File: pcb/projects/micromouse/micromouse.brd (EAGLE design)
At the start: 80 x 100 mm, 45 parts, among them U1 DSPIC33FJ64MC804-H/PTTQFP44_1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, U2 UA78M33CKCS, U3 UA78M05CKCS

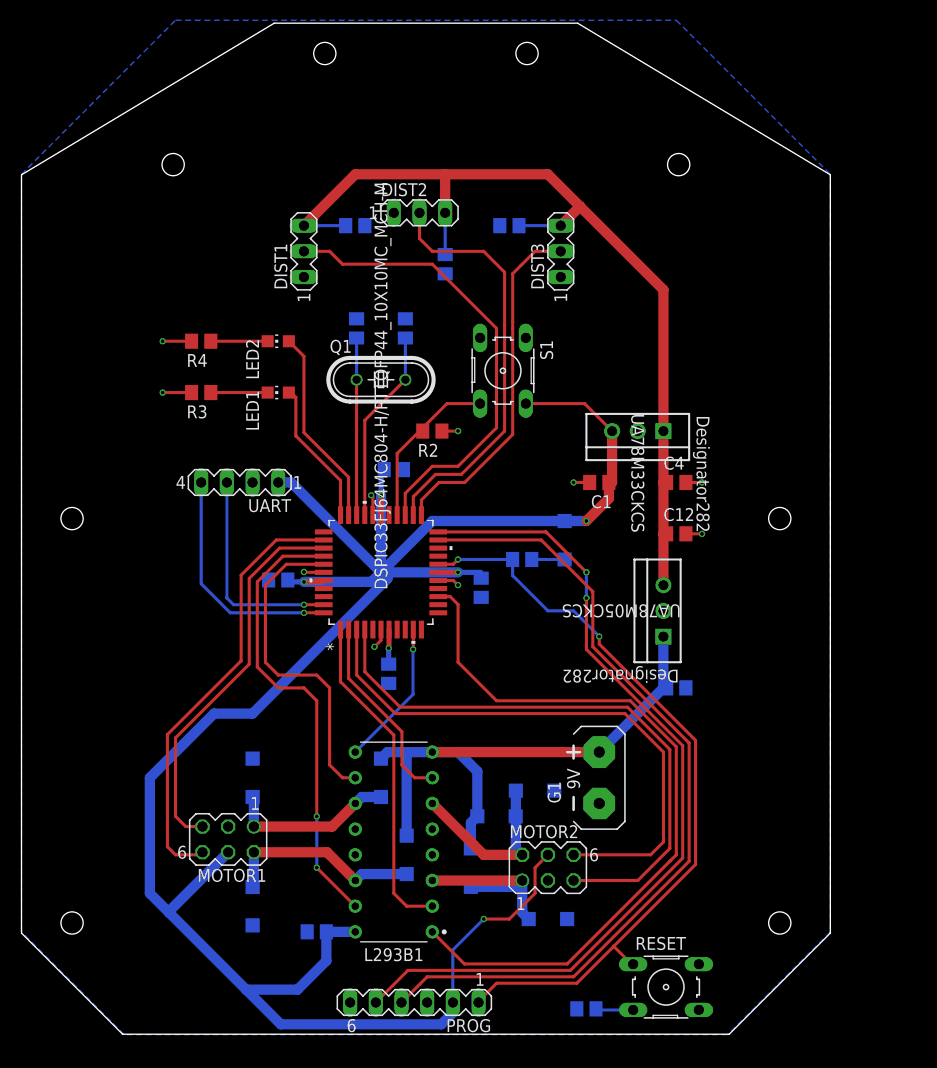
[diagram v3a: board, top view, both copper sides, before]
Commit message: Update reset button
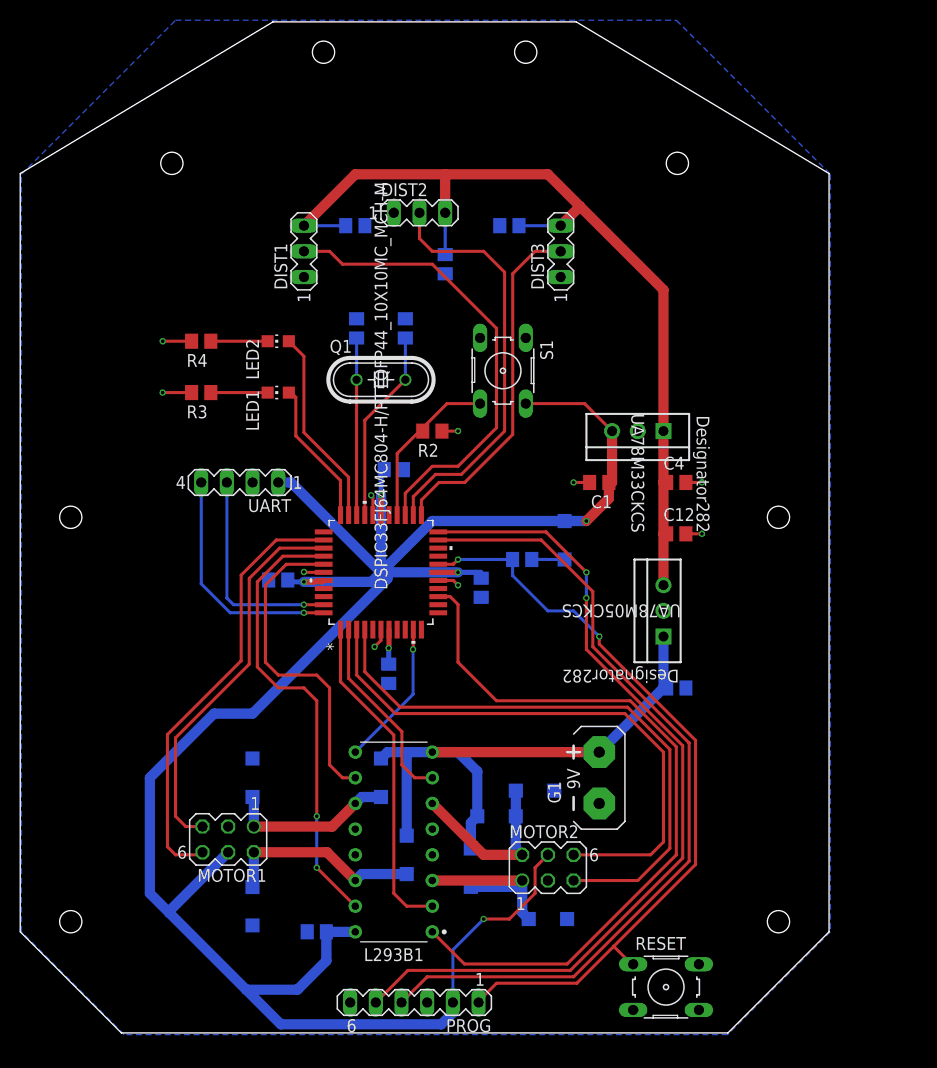
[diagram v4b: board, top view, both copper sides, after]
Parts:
- removed C8: 100nF, rcl:C0805
- R1: value 10k -> 47k
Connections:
- removed net N$3: C8.1, RESET.3
- net GND: now also RESET.3; no longer C8.2
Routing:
- net N$3: track 3.71 -> 0.00 mm
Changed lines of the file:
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@@
 <setting verticaltext="up"/>
 </settings>
-<grid distance="50" unitdist="mil" unit="mil" style="dots" multiple="1" display="yes" altdistance="5" altunitdist="mil" altunit="mil"/>
+<grid distance="50" unitdist="mil" unit="mm" style="dots" multiple="1" display="yes" altdistance="5" altunitdist="mil" altunit="mm"/>
 <layers>
 <layer number="1" name="Top" color="4" fill="1" visible="yes" active="yes"/>
@@
 </layers>
 <board>
-<fusionsync huburn="a.YnVzaW5lc3M6bXl0dW03NTE" projecturn="a.YnVzaW5lc3M6bXl0dW03NTEjMjAyMjAxMTg0ODY2MTA4MzE" f3durn="urn:adsk.wipprod:dm.lineage:keifWLGXSk6oYHrA5SEV4A" pcbguid="" lastpulledtime="2022-01-28T17:10:11Z" lastsyncedchangeguid="" latestrevisionid="4de54440-2fe9-4c7d-ae27-a806fae1d480" lastsyncedrevisionid="4de54440-2fe9-4c7d-ae27-a806fae1d480" lastboardhashguid="1363f738-ee43-156e-3d66-bee1ae0f74bd" lastpushedtime="2022-01-31T12:11:03Z" linktopcb3d="true"/>
+<fusionsync huburn="a.YnVzaW5lc3M6bXl0dW03NTE" projecturn="a.YnVzaW5lc3M6bXl0dW03NTEjMjAyMjAxMTg0ODY2MTA4MzE" f3durn="urn:adsk.wipprod:dm.lineage:keifWLGXSk6oYHrA5SEV4A" pcbguid="" lastpulledtime="2022-02-01T13:51:11Z" lastsyncedchangeguid="" latestrevisionid="4de54440-2fe9-4c7d-ae27-a806fae1d480" lastsyncedrevisionid="d05ad1f5-a34a-4595-a2cb-2618f3431890" lastboardhashguid="1363f738-ee43-156e-3d66-bee1ae0f74bd" lastpushedtime="2022-01-31T12:11:03Z" linktopcb3d="true"/>
 <plain>
 <wire x1="10.16" y1="0" x2="10.16" y2="69.85" width="0.1524" layer="48" style="shortdash"/>
@@
 because parts will be mounted
 there.</text>
-<circle x="75.005" y="11.038" locked="yes" radius="1.1" width="0" layer="20"/>
-<circle x="5.005" y="51.038" locked="yes" radius="1.1" width="0" layer="20"/>
-<circle x="30.005" y="97.038" locked="yes" radius="1.1" width="0" layer="20"/>
-<circle x="15.005" y="86.047" locked="yes" radius="1.1" width="0" layer="20"/>
-<circle x="5.005" y="11.038" locked="yes" radius="1.1" width="0" layer="20"/>
-<circle x="75.005" y="51.038" locked="yes" radius="1.1" width="0" layer="20"/>
-<circle x="50.005" y="97.038" locked="yes" radius="1.1" width="0" layer="20"/>
-<circle x="65.005" y="86.047" locked="yes" radius="1.1" width="0" layer="20"/>
-<wire x1="70.005" y1="0.038" x2="80.005" y2="10.038" width="0" layer="20" locked="yes"/>
-<wire x1="80.005" y1="10.038" x2="80.005" y2="85.038" width="0" layer="20" locked="yes"/>
-<wire x1="55.005" y1="100.038" x2="80.005" y2="85.038" width="0" layer="20" locked="yes"/>
-<wire x1="55.005" y1="100.038" x2="25.005" y2="100.038" width="0" layer="20" locked="yes"/>
-<wire x1="25.005" y1="100.038" x2="0.005" y2="85.038" width="0" layer="20" locked="yes"/>
-<wire x1="0.005" y1="10.038" x2="0.005" y2="85.038" width="0" layer="20" locked="yes"/>
-<wire x1="10.005" y1="0.038" x2="0.005" y2="10.038" width="0" layer="20" locked="yes"/>
-<wire x1="70.005" y1="0.038" x2="10.005" y2="0.038" width="0" layer="20" locked="yes"/>
+<circle x="74.878" y="11.165" radius="1.1" width="0" layer="20"/>
+<circle x="4.878" y="51.165" radius="1.1" width="0" layer="20"/>
+<circle x="29.878" y="97.165" radius="1.1" width="0" layer="20"/>
+<circle x="14.878" y="86.174" radius="1.1" width="0" layer="20"/>
+<circle x="4.878" y="11.165" radius="1.1" width="0" layer="20"/>
+<circle x="74.878" y="51.165" radius="1.1" width="0" layer="20"/>
+<circle x="49.878" y="97.165" radius="1.1" width="0" layer="20"/>
+<circle x="64.878" y="86.174" radius="1.1" width="0" layer="20"/>
+<wire x1="69.878" y1="0.165" x2="79.878" y2="10.165" width="0" layer="20"/>
+<wire x1="79.878" y1="10.165" x2="79.878" y2="85.165" width="0" layer="20"/>
+<wire x1="54.878" y1="100.165" x2="79.878" y2="85.165" width="0" layer="20"/>
+<wire x1="54.878" y1="100.165" x2="24.878" y2="100.165" width="0" layer="20"/>
+<wire x1="24.878" y1="100.165" x2="-0.122" y2="85.165" width="0" layer="20"/>
+<wire x1="-0.122" y1="10.165" x2="-0.122" y2="85.165" width="0" layer="20"/>
+<wire x1="9.878" y1="0.165" x2="-0.122" y2="10.165" width="0" layer="20"/>
+<wire x1="69.878" y1="0.165" x2="9.878" y2="0.165" width="0" layer="20"/>
 </plain>
 <attributes>
@@
 <attribute name="VALUE" x="31.75" y="82.55" size="1.27" layer="28" rot="MR180"/>
 </element>
-<element name="C8" library="rcl" library_urn="urn:adsk.eagle:library:334" package="C0805" package3d_urn="urn:adsk.eagle:package:23617/2" value="100nF" x="55.88" y="2.54" smashed="yes" rot="MR0">
-<attribute name="NAME" x="57.15" y="3.81" size="1.27" layer="26" rot="MR0"/>
-<attribute name="POPULARITY" value="88" x="12.7" y="-71.12" size="1.778" layer="28" rot="MR0" display="off"/>
-<attribute name="SPICEPREFIX" value="C" x="12.7" y="-71.12" size="1.778" layer="28" rot="MR0" display="off"/>
-<attribute name="VALUE" x="57.15" y="0" size="1.27" layer="28" rot="MR0"/>
-</element>
 <element name="C9" library="rcl" library_urn="urn:adsk.eagle:library:334" package="C0805" package3d_urn="urn:adsk.eagle:package:23617/2" value="100nF" x="41.91" y="76.2" smashed="yes" rot="MR270">
 <attribute name="NAME" x="40.64" y="77.47" size="1.27" layer="26" rot="MR270"/>
@@
 <attribute name="VALUE" x="30.48" y="60.833" size="1.27" layer="27" ratio="10"/>
 </element>
-<element name="R1" library="rcl" library_urn="urn:adsk.eagle:library:334" package="R0805" package3d_urn="urn:adsk.eagle:package:23553/2" value="10k" x="49.53" y="46.99" smashed="yes" rot="MR180">
+<element name="R1" library="rcl" library_urn="urn:adsk.eagle:library:334" package="R0805" package3d_urn="urn:adsk.eagle:package:23553/2" value="47k" x="49.53" y="46.99" smashed="yes" rot="MR180">
 <attribute name="NAME" x="48.895" y="45.72" size="1.27" layer="26" rot="MR180"/>
 <attribute name="POPULARITY" value="86" x="123.19" y="115.57" size="1.778" layer="28" rot="MR180" display="off"/>
@@
 <contactref element="C5" pad="1"/>
 <contactref element="U1" pad="6"/>
-<contactref element="C8" pad="2"/>
 <contactref element="U1" pad="16"/>
 <contactref element="U1" pad="29"/>
@@
 <vertex x="69.85" y="0"/>
 </polygon>
+<contactref element="RESET" pad="3"/>
 </signal>
 <signal name="MCLR">
@@
 <wire x1="43.18" y1="42.545" x2="42.405" y2="43.32" width="0.3048" layer="1"/>
 <wire x1="43.815" y1="6.985" x2="53.975" y2="6.985" width="0.3048" layer="1"/>
-<wire x1="53.975" y1="6.985" x2="64.135" y2="17.145" width="0.3048" layer="1"/>
-<wire x1="64.135" y1="17.145" x2="64.13500625" y2="17.14500625" width="0.3048" layer="1"/>
-<wire x1="64.13500625" y1="17.14500625" x2="64.77" y2="17.78" width="0.3048" layer="1"/>
+<wire x1="53.975" y1="6.985" x2="64.77" y2="17.78" width="0.3048" layer="1"/>
 </signal>
 <signal name="M2_D1">
@@
 <wire x1="43.511375" y1="55.41" x2="47.79" y2="59.688625" width="0.3048" layer="1"/>
 <wire x1="40.964625" y1="55.41" x2="43.511375" y2="55.41" width="0.3048" layer="1"/>
-<wire x1="47.79" y1="59.688625" x2="47.79" y2="69.85" width="0.3048" layer="1"/>
-<wire x1="47.79" y1="69.85" x2="47.79" y2="70.181375" width="0.3048" layer="1"/>
+<wire x1="47.79" y1="59.688625" x2="47.79" y2="75.4" width="0.3048" layer="1"/>
 <wire x1="40.64" y1="77.47" x2="39.37" y2="78.74" width="0.3048" layer="1"/>
-<wire x1="47.79" y1="70.181375" x2="47.79" y2="75.4" width="0.3048" layer="1"/>
 <wire x1="47.79" y1="75.4" x2="45.72" y2="77.47" width="0.3048" layer="1"/>
 <wire x1="45.72" y1="77.47" x2="40.64" y2="77.47" width="0.3048" layer="1"/>
@@
 <wire x1="43.84275" y1="54.61" x2="48.59" y2="59.35725" width="0.3048" layer="1"/>
 <wire x1="41.296003125" y1="54.61" x2="43.84275" y2="54.61" width="0.3048" layer="1"/>
-<wire x1="48.59" y1="59.35725" x2="48.59" y2="69.85" width="0.3048" layer="1"/>
-<wire x1="48.59" y1="69.85" x2="48.59" y2="70.51275" width="0.3048" layer="1"/>
-<wire x1="49.391375" y1="76.061375" x2="49.53" y2="76.2" width="0.3048" layer="1"/>
-<wire x1="49.53" y1="76.2" x2="50.8" y2="77.47" width="0.3048" layer="1"/>
+<wire x1="48.59" y1="59.35725" x2="48.59" y2="75.26" width="0.3048" layer="1"/>
+<wire x1="48.59" y1="75.26" x2="50.8" y2="77.47" width="0.3048" layer="1"/>
 <wire x1="50.8" y1="77.47" x2="53.34" y2="77.47" width="0.3048" layer="1"/>
-<wire x1="48.59" y1="70.51275" x2="48.59" y2="75.26" width="0.3048" layer="1"/>
-<wire x1="48.59" y1="75.26" x2="49.391375" y2="76.061375" width="0.3048" layer="1"/>
 </signal>
 <signal name="VCAP">
@@
 <contactref element="R4" pad="1"/>
 <wire x1="24.35" y1="68.58" x2="18.73" y2="68.58" width="0.3048" layer="1"/>
-</signal>
-<signal name="N$3">
-<contactref element="RESET" pad="3"/>
-<contactref element="C8" pad="1"/>
-<wire x1="60.5028" y1="2.4384" x2="56.9316" y2="2.4384" width="0.3048" layer="16"/>
-<wire x1="56.9316" y1="2.4384" x2="56.83" y2="2.54" width="0.3048" layer="16"/>
 </signal>
 </signals>
@@
 packages will not be understood (or retained) with this version.
 </note>
-<note version="8.5" severity="warning">
-Since Version 8.5, EAGLE supports locking for holes, vias, wires and polygons.
-The locking property on all objects of these types will not be understood in this version.
-</note>
 </compatibility>

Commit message: LED and resistor value
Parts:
- added LED3: (no value), led:LED3MM
- R2: value (none) -> 10k
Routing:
- net +5V: track 91.1 -> 88.8 mm
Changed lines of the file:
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@@
 <attribute name="VALUE" x="48.895" y="49.53" size="1.27" layer="28" rot="MR180"/>
 </element>
-<element name="R2" library="rcl" library_urn="urn:adsk.eagle:library:334" package="R0805" package3d_urn="urn:adsk.eagle:package:23553/2" value="" x="40.64" y="59.69" smashed="yes" rot="R180">
+<element name="R2" library="rcl" library_urn="urn:adsk.eagle:library:334" package="R0805" package3d_urn="urn:adsk.eagle:package:23553/2" value="10k" x="40.64" y="59.69" smashed="yes" rot="R180">
 <attribute name="NAME" x="41.275" y="58.42" size="1.27" layer="25" rot="R180"/>
 <attribute name="POPULARITY" value="86" x="2.54" y="133.35" size="1.778" layer="27" rot="R180" display="off"/>
@@
 <attribute name="POPULARITY" value="32" x="57.15" y="25.4" size="1.778" layer="27" display="off"/>
 <attribute name="VALUE" x="61.595" y="22.86" size="1.27" layer="27" ratio="10" rot="R90"/>
+</element>
+<element name="LED3" library="led" library_urn="urn:adsk.eagle:library:259" package="LED3MM" package3d_urn="urn:adsk.eagle:package:15797/1" value="" x="39.37" y="86.36" smashed="yes" rot="MR0">
+<attribute name="NAME" x="36.195" y="86.8934" size="1.27" layer="26" ratio="10" rot="MR0"/>
+<attribute name="POPULARITY" value="97" x="39.37" y="86.36" size="1.778" layer="28" rot="MR0" display="off"/>
+<attribute name="VALUE" x="36.1696" y="84.5566" size="1.27" layer="28" ratio="10" rot="MR0"/>
 </element>
 </elements>
@@
 <wire x1="63.5" y1="59.69" x2="63.5" y2="73.66" width="1.016" layer="1"/>
 <wire x1="63.5" y1="73.66" x2="55.245" y2="81.915" width="1.016" layer="1"/>
-<wire x1="55.245" y1="81.915" x2="52.07" y2="85.09" width="1.016" layer="1"/>
-<wire x1="52.07" y1="85.09" x2="41.91" y2="85.09" width="1.016" layer="1"/>
-<wire x1="41.91" y1="85.09" x2="33.02" y2="85.09" width="1.016" layer="1"/>
-<wire x1="33.02" y1="85.09" x2="27.94" y2="80.01" width="1.016" layer="1"/>
-<wire x1="41.91" y1="85.09" x2="41.91" y2="81.28" width="1.016" layer="1"/>
+<wire x1="55.245" y1="81.915" x2="53.34" y2="83.82" width="1.016" layer="1"/>
+<wire x1="53.34" y1="83.82" x2="41.91" y2="83.82" width="1.016" layer="1"/>
+<wire x1="41.91" y1="83.82" x2="31.75" y2="83.82" width="1.016" layer="1"/>
+<wire x1="31.75" y1="83.82" x2="27.94" y2="80.01" width="1.016" layer="1"/>
+<wire x1="41.91" y1="83.82" x2="41.91" y2="81.28" width="1.016" layer="1"/>
 <wire x1="27.94" y1="80.01" x2="32.07" y2="80.01" width="0.3048" layer="16"/>
 <wire x1="41.91" y1="81.28" x2="41.91" y2="77.15" width="0.3048" layer="16"/>

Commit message: Update
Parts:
- removed LED3: (no value), led:LED3MM
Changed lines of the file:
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@@
 <setting verticaltext="up"/>
 </settings>
-<grid distance="50" unitdist="mil" unit="mm" style="dots" multiple="1" display="yes" altdistance="5" altunitdist="mil" altunit="mm"/>
+<grid distance="50" unitdist="mil" unit="mil" style="dots" multiple="1" display="yes" altdistance="5" altunitdist="mil" altunit="mil"/>
 <layers>
 <layer number="1" name="Top" color="4" fill="1" visible="yes" active="yes"/>
@@
 </element>
 <element name="C14" library="rcl" library_urn="urn:adsk.eagle:library:334" package="C0805" package3d_urn="urn:adsk.eagle:package:23617/2" value="100nF" x="36.83" y="55.88" smashed="yes" rot="MR180">
-<attribute name="NAME" x="35.56" y="54.61" size="1.27" layer="26" rot="MR180"/>
 <attribute name="POPULARITY" value="88" x="67.31" y="124.46" size="1.778" layer="28" rot="MR180" display="off"/>
 <attribute name="SPICEPREFIX" value="C" x="67.31" y="124.46" size="1.778" layer="28" rot="MR180" display="off"/>
@@
 <attribute name="POPULARITY" value="32" x="57.15" y="25.4" size="1.778" layer="27" display="off"/>
 <attribute name="VALUE" x="61.595" y="22.86" size="1.27" layer="27" ratio="10" rot="R90"/>
-</element>
-<element name="LED3" library="led" library_urn="urn:adsk.eagle:library:259" package="LED3MM" package3d_urn="urn:adsk.eagle:package:15797/1" value="" x="39.37" y="86.36" smashed="yes" rot="MR0">
-<attribute name="NAME" x="36.195" y="86.8934" size="1.27" layer="26" ratio="10" rot="MR0"/>
-<attribute name="POPULARITY" value="97" x="39.37" y="86.36" size="1.778" layer="28" rot="MR0" display="off"/>
-<attribute name="VALUE" x="36.1696" y="84.5566" size="1.27" layer="28" ratio="10" rot="MR0"/>
 </element>
 </elements>
@@
 <wire x1="58.1" y1="54.61" x2="58.1" y2="53.02" width="1.016" layer="1"/>
 <wire x1="58.1" y1="53.02" x2="55.88" y2="50.8" width="1.016" layer="1"/>
-<wire x1="35.56" y1="55.56" x2="35.72" y2="55.72" width="0.3048" layer="16"/>
-<wire x1="35.72" y1="55.72" x2="35.88" y2="55.88" width="0.3048" layer="16"/>
 <wire x1="41.2234" y1="45.72" x2="43.18" y2="45.72" width="0.508" layer="1"/>
 <wire x1="45.466" y1="45.146" x2="45.44673125" y2="45.72" width="0.3048" layer="16"/>
@@
 <wire x1="35.56" y1="52.922425" x2="35.5704" y2="52.932825" width="1.016" layer="16"/>
 <wire x1="35.5704" y1="52.932825" x2="35.5704" y2="53.34" width="1.016" layer="16"/>
-<wire x1="35.5704" y1="53.34" x2="35.5704" y2="55.5704" width="0.508" layer="16"/>
-<wire x1="35.5704" y1="55.5704" x2="35.72" y2="55.72" width="0.508" layer="16"/>
 <wire x1="35.56" y1="51.3834" x2="35.56" y2="53.3296" width="0.508" layer="1"/>
 <wire x1="35.56" y1="53.3296" x2="35.5704" y2="53.34" width="0.508" layer="1"/>
 <via x="35.5704" y="53.34" extent="1-16" drill="0.35"/>
+<wire x1="35.5704" y1="53.34" x2="35.5704" y2="55.5704" width="0.508" layer="16"/>
+<wire x1="35.5704" y1="55.5704" x2="35.88" y2="55.88" width="0.508" layer="16"/>
 </signal>
 <signal name="+9V">

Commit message: Updates
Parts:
- added C16, C8: 100nF, rcl:C0805
- added LED3: (no value), led:LED5MM
- C1: value 100nF -> 10nF (T)
- C4: value .33uF -> 10uF
- C5: value 4.7uF -> 4.7uF (T)
- R1: value 47k -> 4.7k
- moved C1 1.27 mm to (55.9, 54.6)
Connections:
- net GND: now also C16.2, C8.2
- net VDD: now also C16.1, C8.1
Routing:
- net VDD: track 216.8 -> 221.6 mm

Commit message: Final PCB touches
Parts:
- renumbered S1 to BUTTON, U1 to DSPIC33FJ64MC804, U2 to LM1085IT-3.3, U3 to UA78M05
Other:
- board text added: "EA VDD M+"
- board text added: "EB GND"
- board text added: "GND EB"
- board text added: "GND SEN +5V"
- board text added: "M+ VDD"
- board text added: "Minimaus WS 2021/22 Miriam Welser Michelle Bettendorf Marius Kleidl Joshua Wendland Made with little experience. Let's hope it works."
- board text added: "RX TX GND VDD"
